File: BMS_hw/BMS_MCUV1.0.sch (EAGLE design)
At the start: 0 parts

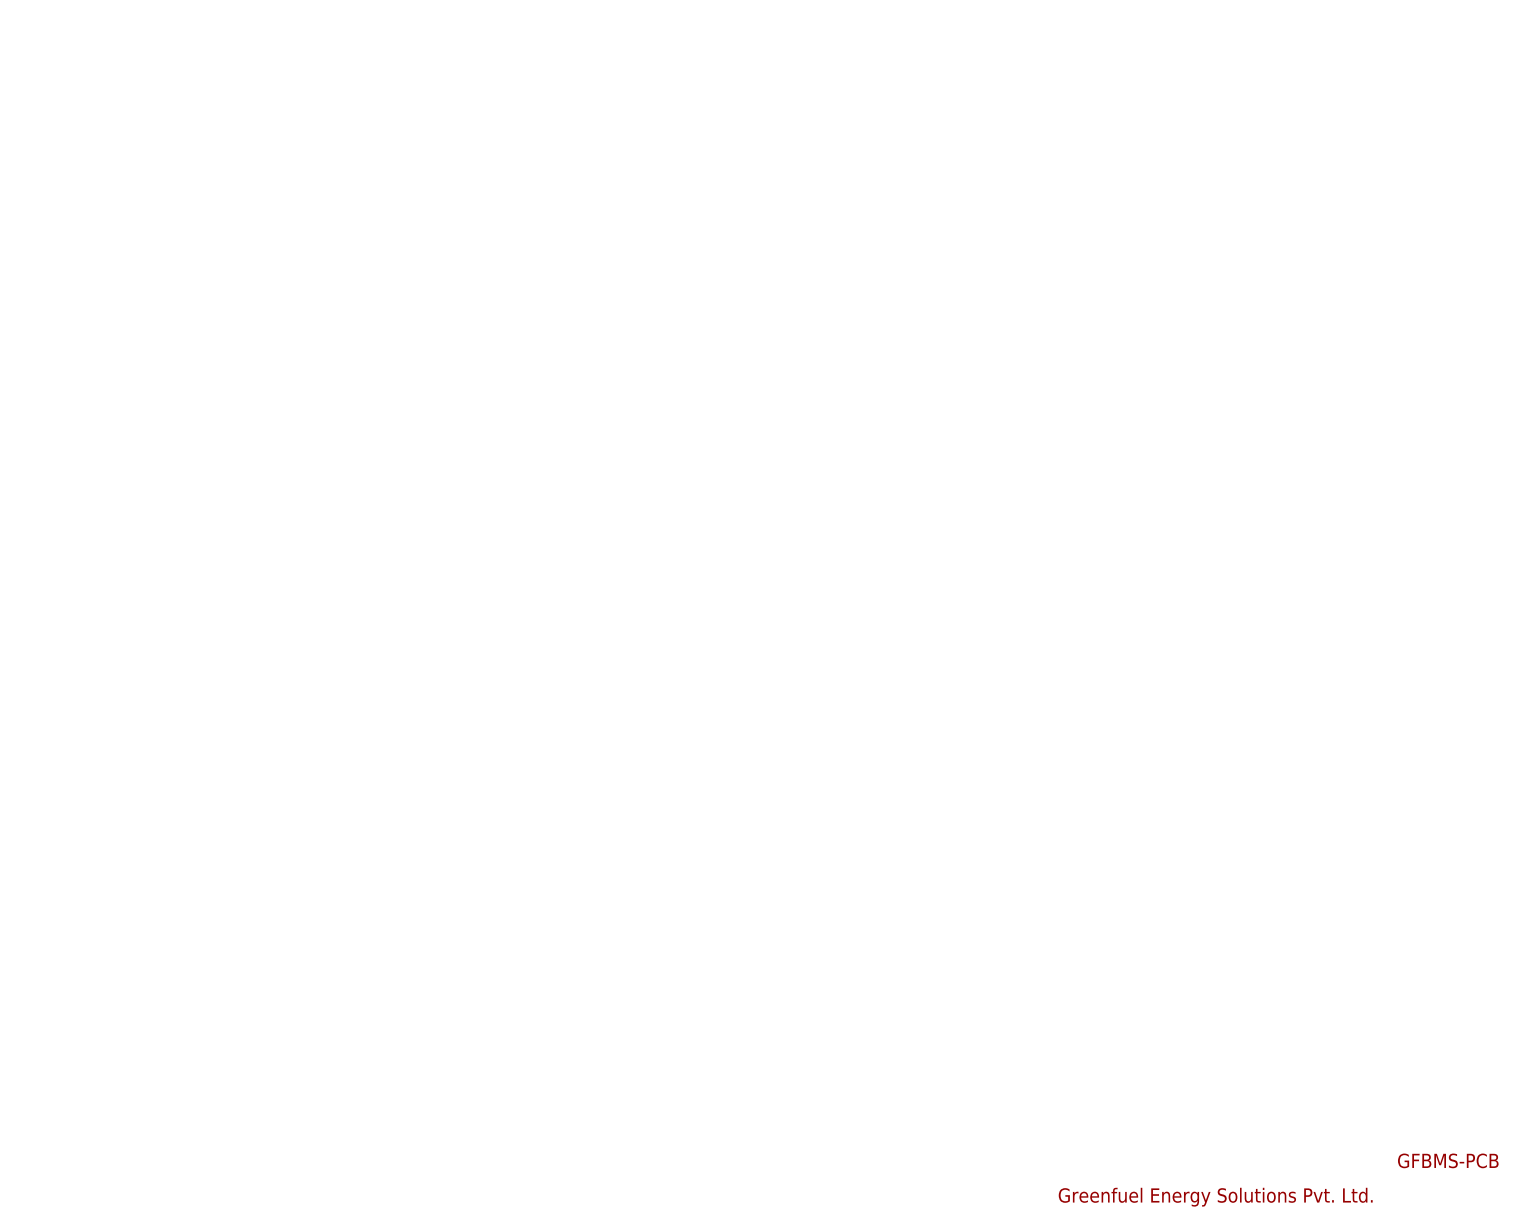
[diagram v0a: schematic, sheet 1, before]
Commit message: MCU placed sch
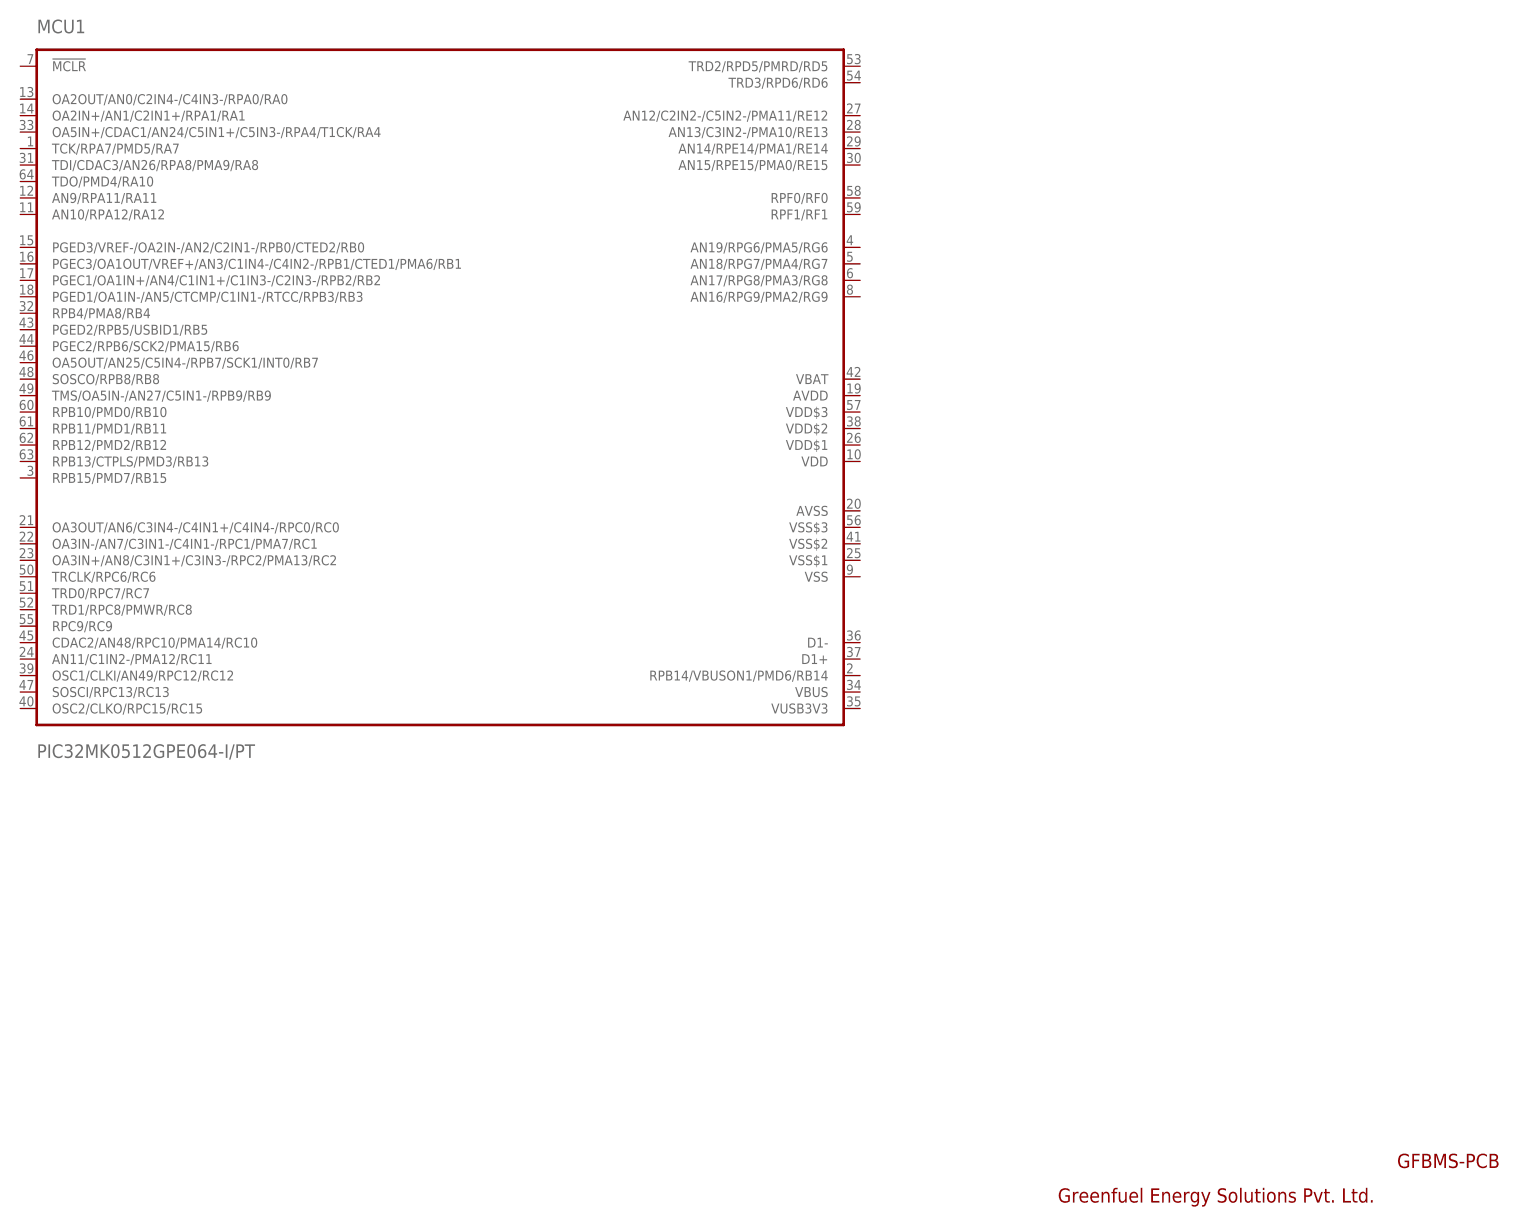
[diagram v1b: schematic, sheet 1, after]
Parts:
- added MCU1: PIC32MK0512GPE064-I/PT, GreenFuel:PIC32MK0512GPE064-I/PT
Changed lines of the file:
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@@
 <setting verticaltext="up"/>
 </settings>
-<grid distance="0.1" unitdist="inch" unit="inch" style="lines" multiple="1" display="no" altdistance="0.01" altunitdist="inch" altunit="inch"/>
+<grid distance="0.1" unitdist="inch" unit="inch" style="lines" multiple="1" display="yes" altdistance="0.01" altunitdist="inch" altunit="inch"/>
 <layers>
 <layer number="1" name="Top" color="4" fill="1" visible="no" active="no"/>
@@
 <part name="FRAME1" library="frames" library_urn="urn:adsk.eagle:library:229" deviceset="A3L-LOC" device=""/>
 <part name="FRAME2" library="frames" library_urn="urn:adsk.eagle:library:229" deviceset="A3L-LOC" device=""/>
+<part name="MCU1" library="GreenFuel" deviceset="PIC32MK0512GPE064-I/PT" device=""/>
 </parts>
 <sheets>
@@
 <instances>
 <instance part="FRAME1" gate="G$1" x="0" y="0"/>
+<instance part="MCU1" gate="G$1" x="193.04" y="139.7"/>
 </instances>
 <busses>
